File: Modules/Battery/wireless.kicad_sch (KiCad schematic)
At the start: 35 parts, among them IC1 LSF0204QPWRQ1, IC2 W25Q16JVUXIQ_TR, J1 USB_C_Receptacle_USB2.0, SW1 BOOT, SW2 RESET, U2 USBLC6-2SC6, U3 2.4GHZ_PCB_Antenna_AN043, Y1 ECS-400-10-37B2-CKM-TR

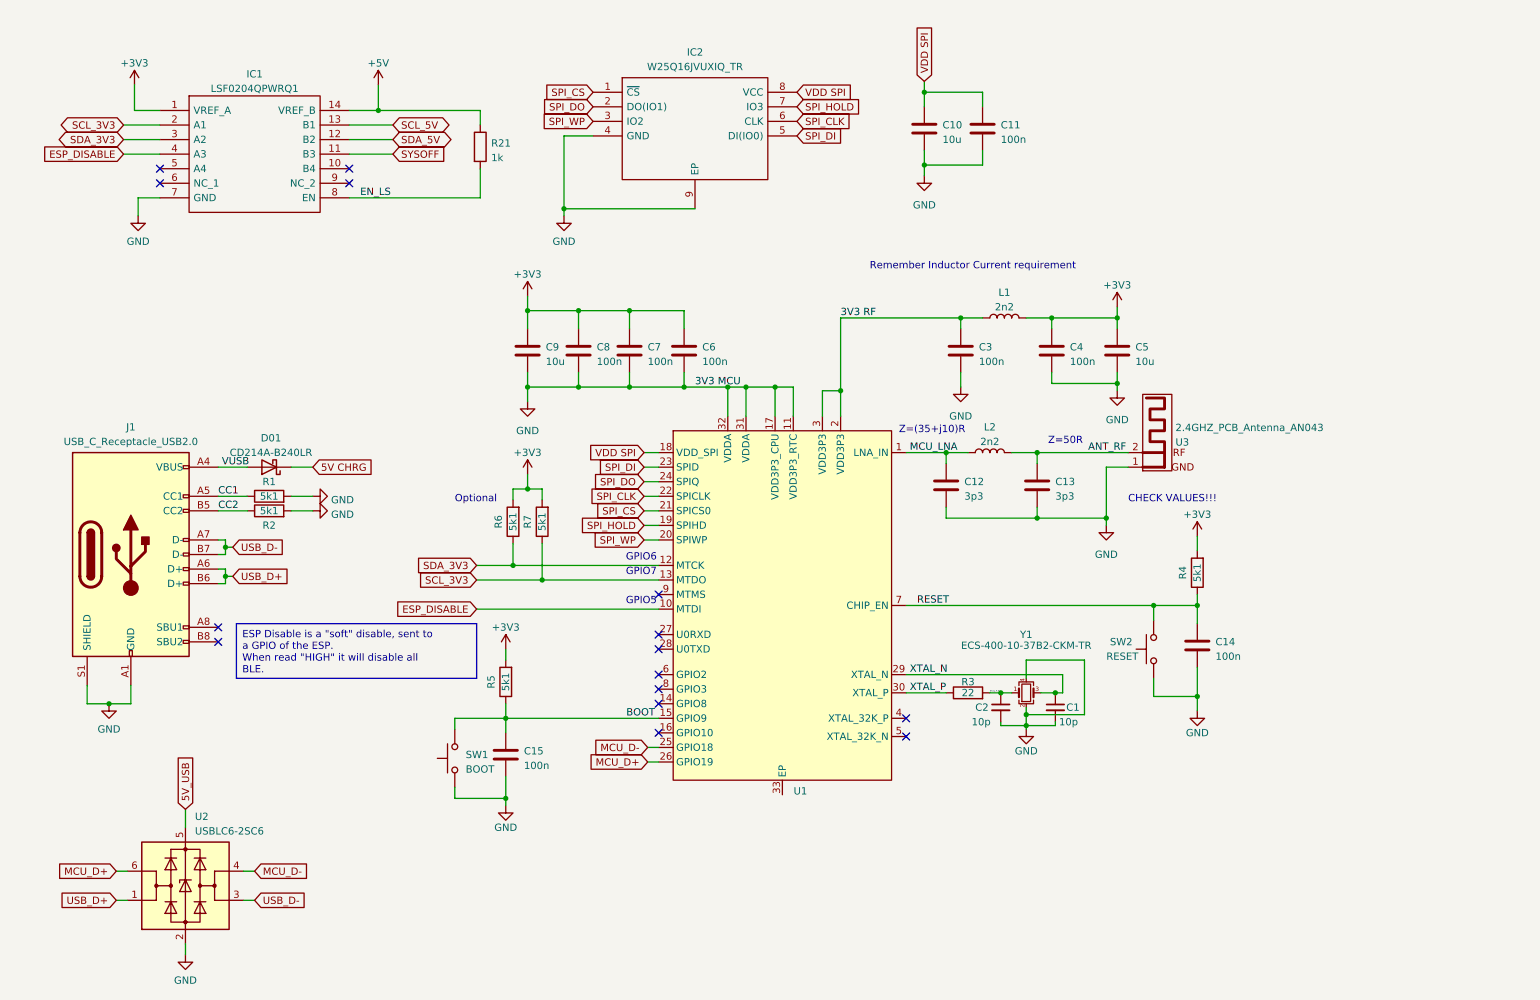
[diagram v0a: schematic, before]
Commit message: update to I2C and MIDI Interface
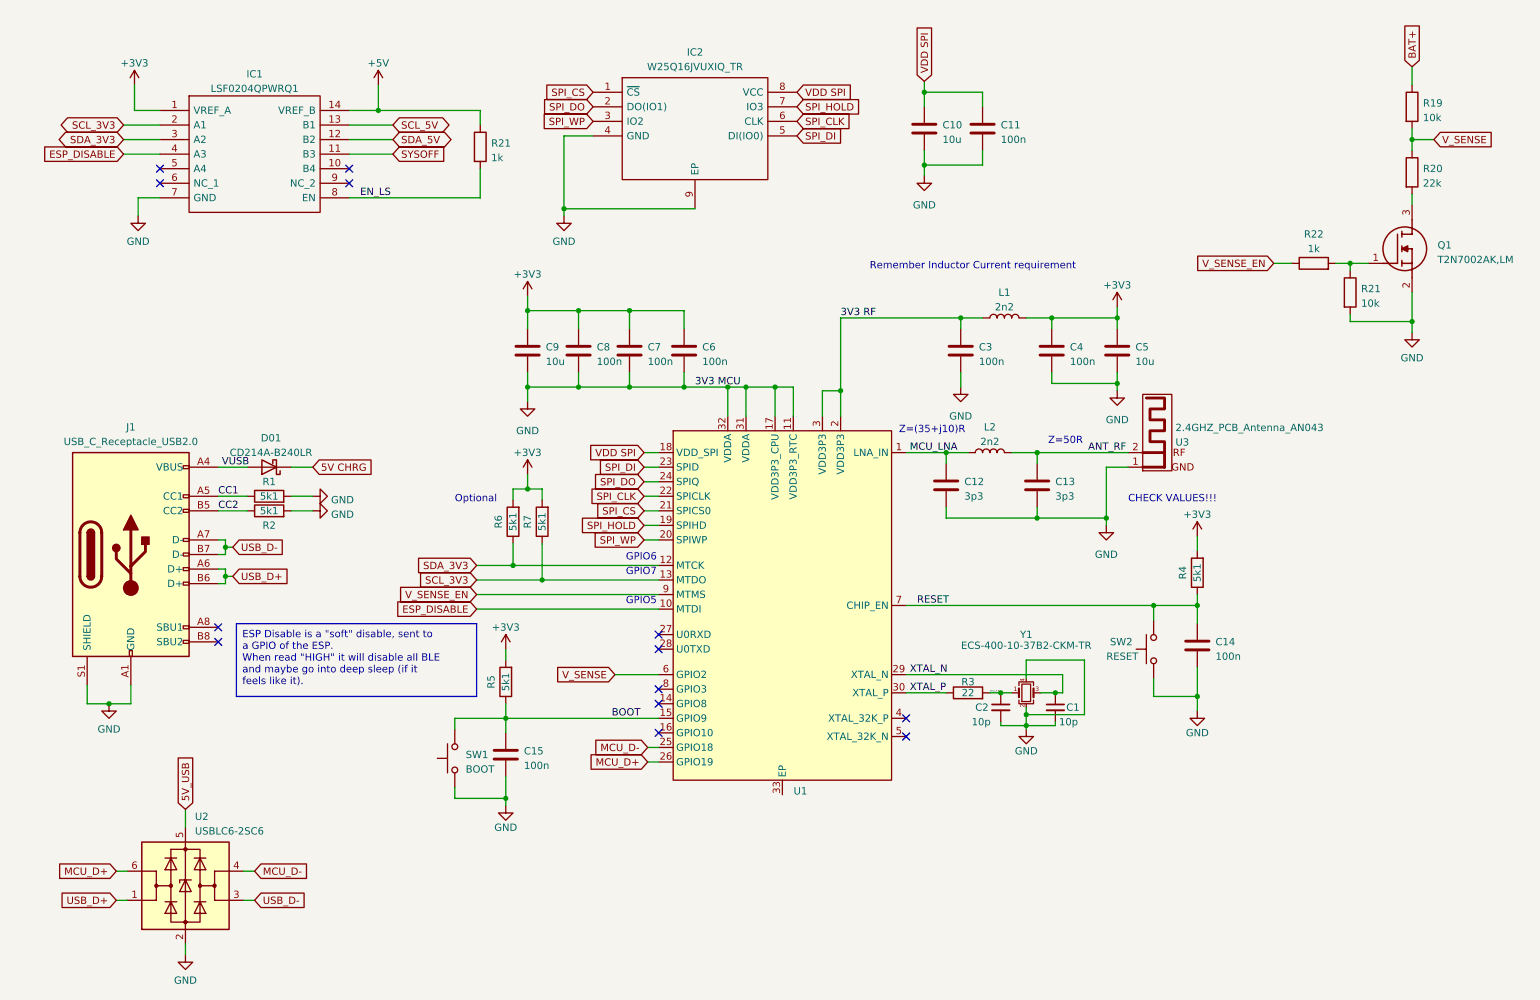
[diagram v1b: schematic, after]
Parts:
- added Q1: T2N7002AK,LM, TBAT54CLM, symbol SamacSys_Parts:T2N7002AK,LM
- added R19, R21: 10k, symbol Device:R
- added R20: 22k, symbol Device:R
- added R22: 1k, symbol Device:R
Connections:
- net GND: now also Q1.2 (S), R21.2
- net V_SENSE: now reaches U1.6 (GPIO2)
- net V_SENSE: now also R19.2, R20.1
- net V_SENSE_EN: now reaches U1.9 (MTMS)
- net V_SENSE_EN: now also R22.1
- new net: Q1.3 (D), R20.2
- new net: Q1.1 (G), R21.1, R22.2
- new net BAT+: R19.1
- no-connect marks 15 -> 13

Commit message: first rev of Battery module
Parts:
- added C29, C30: 100n, Capacitor_SMD:C_0603_1608Metric, symbol Device:C
- added J3: 2337019-1, SamacSys:23370191, symbol SamacSys_Parts:2337019-1
- C1, C10, C11, C12, C13, C14, C15, C2, C3, C4, C5, C6, C7, C8, C9: footprint (none) -> Capacitor_SMD:C_0603_1608Metric
- IC2: footprint SON50P300X200X60-9N -> SamacSys:SON50P300X200X60-9N
- J1: footprint (none) -> Connector_USB:USB_C_Receptacle_GCT_USB4105-xx-A_16P_TopMnt_Horizontal
- L1, L2: footprint (none) -> Inductor_SMD:L_0603_1608Metric
- Q1: footprint TBAT54CLM -> SamacSys:TBAT54CLM
- R1, R19, R2, R20, R21, R22, R3, R4, R5, R6, R7: footprint (none) -> Resistor_SMD:R_0603_1608Metric
- SW1: value BOOT -> PTS636 SP50
- SW2: value RESET -> PTS636 SP50
- U1: value ~ -> ESP32C3
- U3: footprint RF_Antenna:Texas_SWRA117D_2.4GHz_Right -> Antennas:2.4GHZ PCB Antenna AN043; now left out of the parts list
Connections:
- net 5V_USB is gone; now on net VUSB: U2.5 (VBUS)
- net +3V3: now also U1.11 (VDD3P3_RTC), U1.17 (VDD3P3_CPU), U1.31 (VDDA), U1.32 (VDDA), C30.1
- net +5V: now also C29.1
- net ANT_RF: now also U3.1, J3.1 (SIGNAL); no longer U3.2
- net GND: now also U1.33 (EP), U3.2, C29.2, C30.2, J3.2 (GND_1), J3.3 (GND_2); no longer U1.11 (VDD3P3_RTC), U1.17 (VDD3P3_CPU), U1.31 (VDDA), U1.32 (VDDA), U3.1
- net MCU_D+: now also U2.4 (I/O2); no longer U2.6 (I/O1)
- net MCU_D-: now also U2.6 (I/O1); no longer U2.4 (I/O2)
- net USB_D+: now also U2.3 (I/O2); no longer U2.1 (I/O1)
- net USB_D-: now also U2.1 (I/O1); no longer U2.3 (I/O2)
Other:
- note added: "MOSFET Brücken, da sonnst 4.2V an Pin"
- moved on the sheet: IC1, R21, SW2
